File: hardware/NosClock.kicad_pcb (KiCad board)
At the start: 2 copper layers, 144 x 60 mm, 126 parts, among them J101 USB_C_Receptacle_USB2.0_16P, J102 Conn_01x02, J103 Conn_01x04, J104 12V IN, Q301 FQD12N20L, U101 ESP32-C3-MINI-1, U103 DS3231MZ, U201 AP7361-33ER-13, U202 MP2307DN-LF-Z, U301 UC3843_SOIC8, U401 CD4504, U402 SN74LV1T34DBV, U501 HV5222PJ, U601 HV5222PJ, U701 AW9523B

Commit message: finalize v2 tracing
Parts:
- moved BT101 1.32 mm to (98.9, 101.2)
- moved C103 1.28 mm to (89.3, 63.4)
- moved U103 0.75 mm to (82.6, 64.6)
- moved U201 0.47 mm to (182.0, 108.5)
- moved C401 0.33 mm to (84.7, 98.2), turned to 180 degrees
- moved C402 0.20 mm to (84.7, 101.4)
- turned C306 to 0 degrees
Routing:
- net Net-(U301-RC): track 19.4 -> 13.2 mm
- net +5V: track 403.1 -> 399.4 mm
- net GND: track 169.1 -> 166.6 mm
- net /Lamps/ThreeDigits1/SK6812MINI_IN: track 17.9 -> 19.6 mm
- net +12V: track 143.3 -> 145.0 mm
- net /Lamps/ThreeDigits1/LAMP_C2.8: track 27.4 -> 28.5 mm

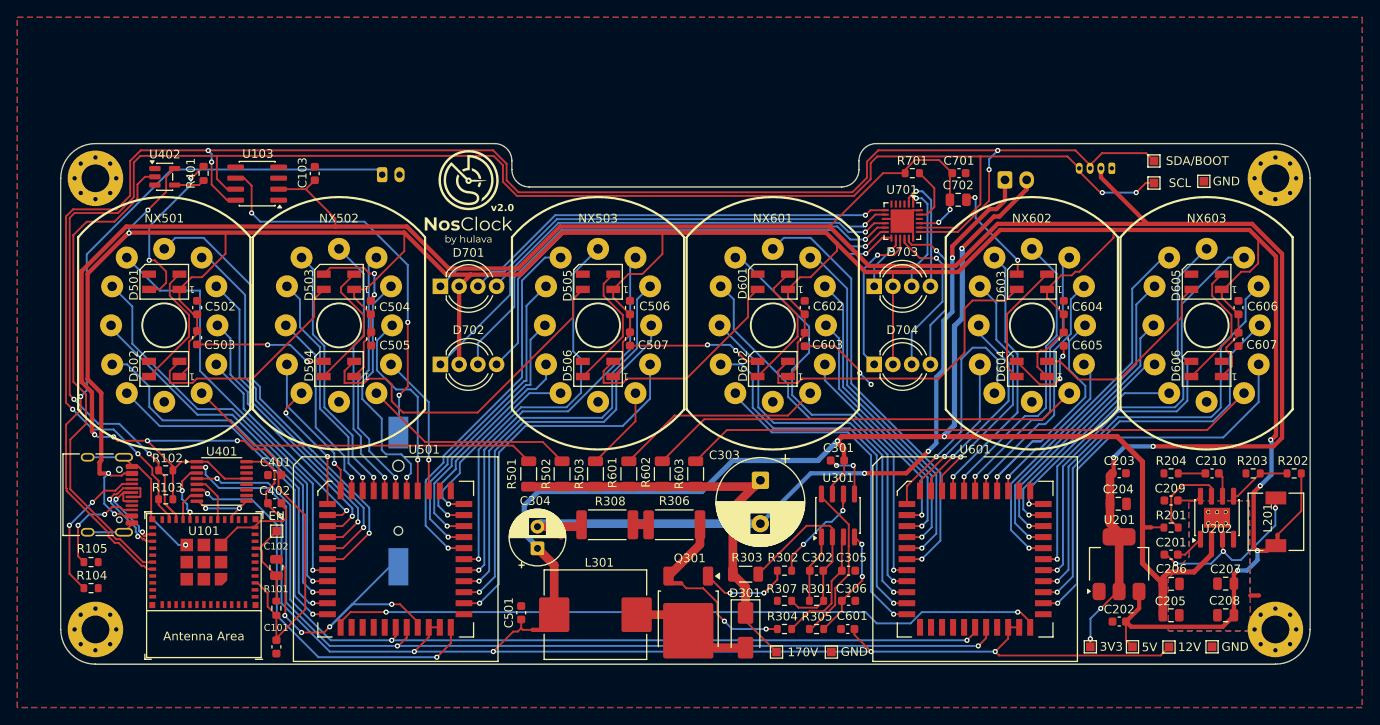
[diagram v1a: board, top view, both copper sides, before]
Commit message: bugfixing
- usb- and usb+ messed up
- wrong boot label
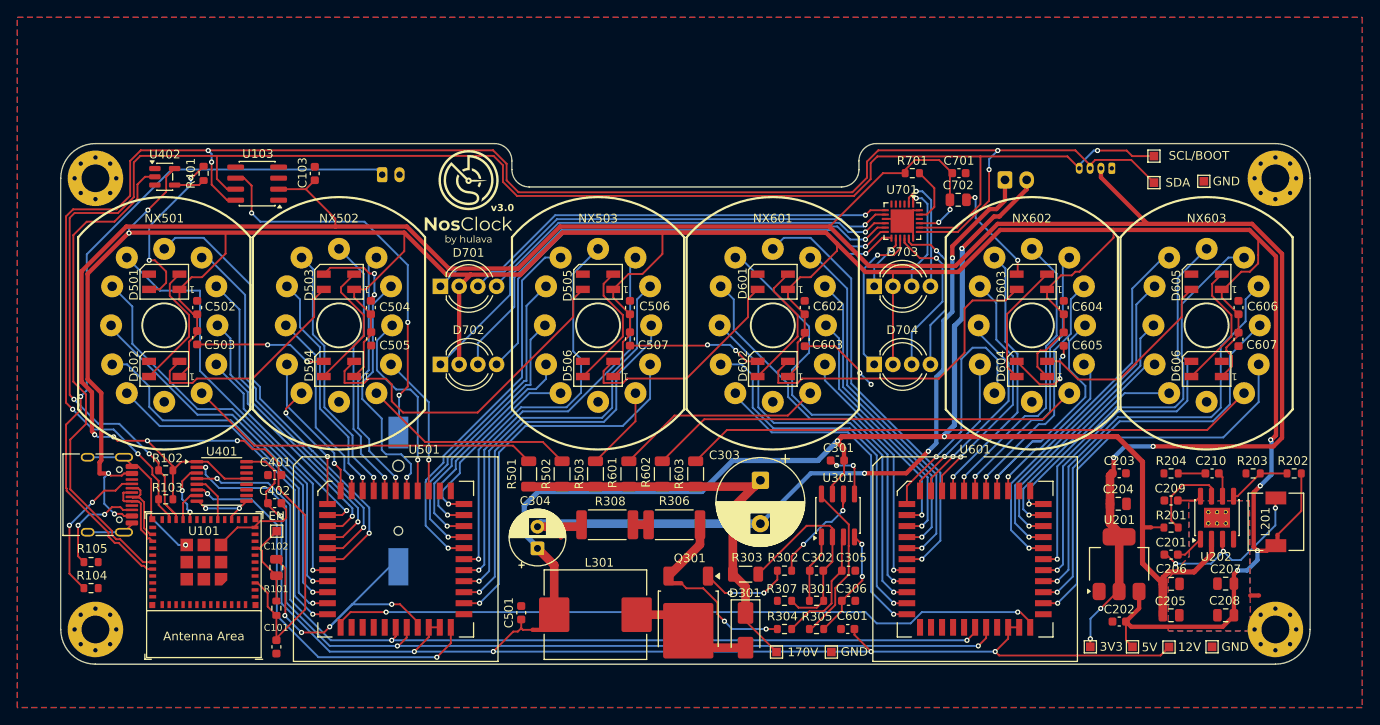
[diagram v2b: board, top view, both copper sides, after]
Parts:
- TP_105: value SDA/BOOT -> SDA
- TP_107: value SCL -> SCL/BOOT
- moved TP_107 3.10 mm to (186.0, 61.4)
- moved TP_105 2.50 mm to (186.0, 64.5)
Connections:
- U101 pad 26: USB_D+ -> USB_D-
- U101 pad 27: USB_D- -> USB_D+
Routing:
- net USB_D-: track 13.5 -> 8.60 mm, vias 2 -> 0
- net USB_D+: track 12.0 -> 9.17 mm, vias 2 -> 0
- net SDA: track 200.6 -> 200.1 mm, vias 4 -> 3
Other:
- board text added: "v3.0"
- board text removed: "v2.0"

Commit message: Fix lamps footprints
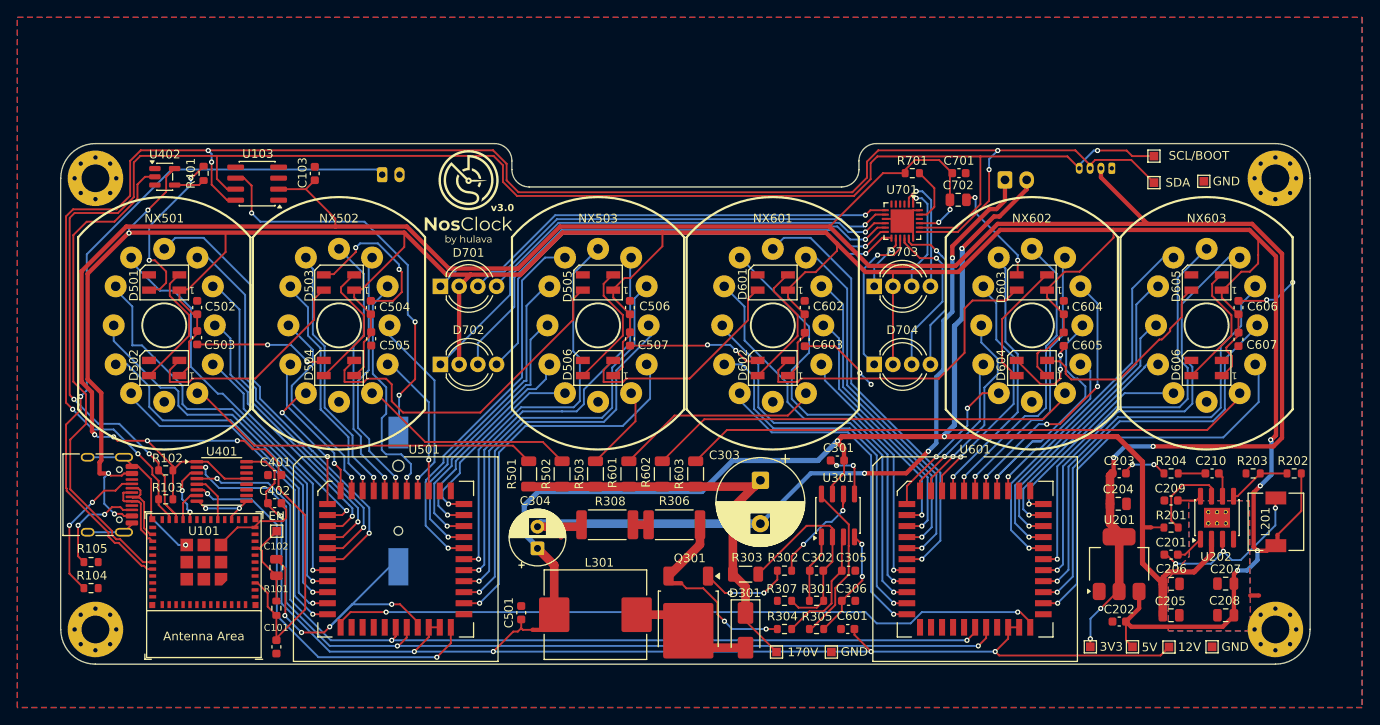
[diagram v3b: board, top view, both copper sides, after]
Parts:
- moved D502 0.11 mm to (71.9, 85.9)
- moved D504 0.11 mm to (92.1, 85.9)
- moved D506 0.11 mm to (121.9, 85.9)
- moved D602 0.11 mm to (142.1, 85.9)
- moved D604 0.11 mm to (171.9, 85.9)
- moved D606 0.11 mm to (192.1, 85.9)
- moved D501 0.08 mm to (71.9, 76.0)
- moved D503 0.08 mm to (92.1, 76.0)
- moved D505 0.08 mm to (121.9, 76.0)
- moved D601 0.08 mm to (142.1, 76.0)
- moved D603 0.08 mm to (171.9, 76.0)
- moved D605 0.08 mm to (192.1, 76.0)
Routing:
- net GND: track 166.6 -> 188.5 mm, vias 21 -> 25
- net /Lamps/ThreeDigits2/LAMP_C2.1: track 28.6 -> 18.3 mm, vias 1 -> 2
- net /Lamps/ThreeDigits2/LAMP_C2.8: track 28.7 -> 31.1 mm, vias 1 -> 3
- net /Lamps/ThreeDigits1/LAMP_C2.3: track 22.2 -> 24.1 mm
- net /Lamps/ThreeDigits1/LAMP_C1.3: track 44.4 -> 46.0 mm
- net /Lamps/ThreeDigits1/LAMP_C1.5: track 49.3 -> 47.9 mm
- net /Lamps/ThreeDigits1/LAMP_C1.4: track 47.6 -> 48.9 mm
- net /Lamps/ThreeDigits2/LAMP_C2.3: track 24.2 -> 23.1 mm
- net /Lamps/ThreeDigits2/LAMP_C3.7: track 52.1 -> 53.1 mm
- net +5V: track 399.3 -> 398.4 mm
- net /Lamps/ThreeDigits2/LAMP_C3.6: track 49.0 -> 49.7 mm
- net Net-(BT101-+): track 44.6 -> 45.3 mm
- net /Lamps/ThreeDigits1/LAMP_C3.9: track 46.8 -> 46.1 mm
- net Net-(D604-DOUT): track 23.0 -> 23.7 mm
- net /Lamps/ThreeDigits1/LAMP_C2.9: track 22.7 -> 22.1 mm
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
